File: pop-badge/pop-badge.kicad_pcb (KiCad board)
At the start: 2 copper layers, 129.5 x 101.3 mm, 164 parts, among them J1 Conn_01x05, Q1 S9013, Q2 AO3400A, U1 WS2812-2020, U10 WS2812-2020, U11 WS2812-2020, U12 WS2812-2020, U13 WS2812-2020, U14 WS2812-2020, U15 WS2812-2020, U16 WS2812-2020, U17 WS2812-2020, U18 WS2812-2020, U19 WS2812-2020, U2 WS2812-2020, U20 WS2812-2020, U21 WS2812-2020, U22 WS2812-2020, U23 WS2812-2020, U24 WS2812-2020, U25 WS2812-2020, U26 Pico, U3 WS2812-2020, U4 WS2812-2020, U5 WS2812-2020, U6 WS2812-2020, U7 WS2812-2020, U8 WS2812-2020, U9 WS2812-2020

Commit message: remove button label
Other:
- board text removed: "Button"
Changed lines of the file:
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@@
   (general
     (thickness 1.6)
-    (drawings 27)
+    (drawings 26)
     (tracks 737)
     (zones 0)
@@
       (drillshape 0)
       (scaleselection 1)
-      (outputdirectory ""))
+      (outputdirectory "gerbers"))
   )
   (net 0 "")
@@
     (effects (font (size 1 1) (thickness 0.15)) (justify mirror))
   )
-  (gr_text Button (at 56.134 120.018811 45) (layer B.SilkS)
-    (effects (font (size 0.8 0.8) (thickness 0.16)) (justify mirror))
-  )
   (gr_text LED- (at 53.848 119.762906 45) (layer B.SilkS)

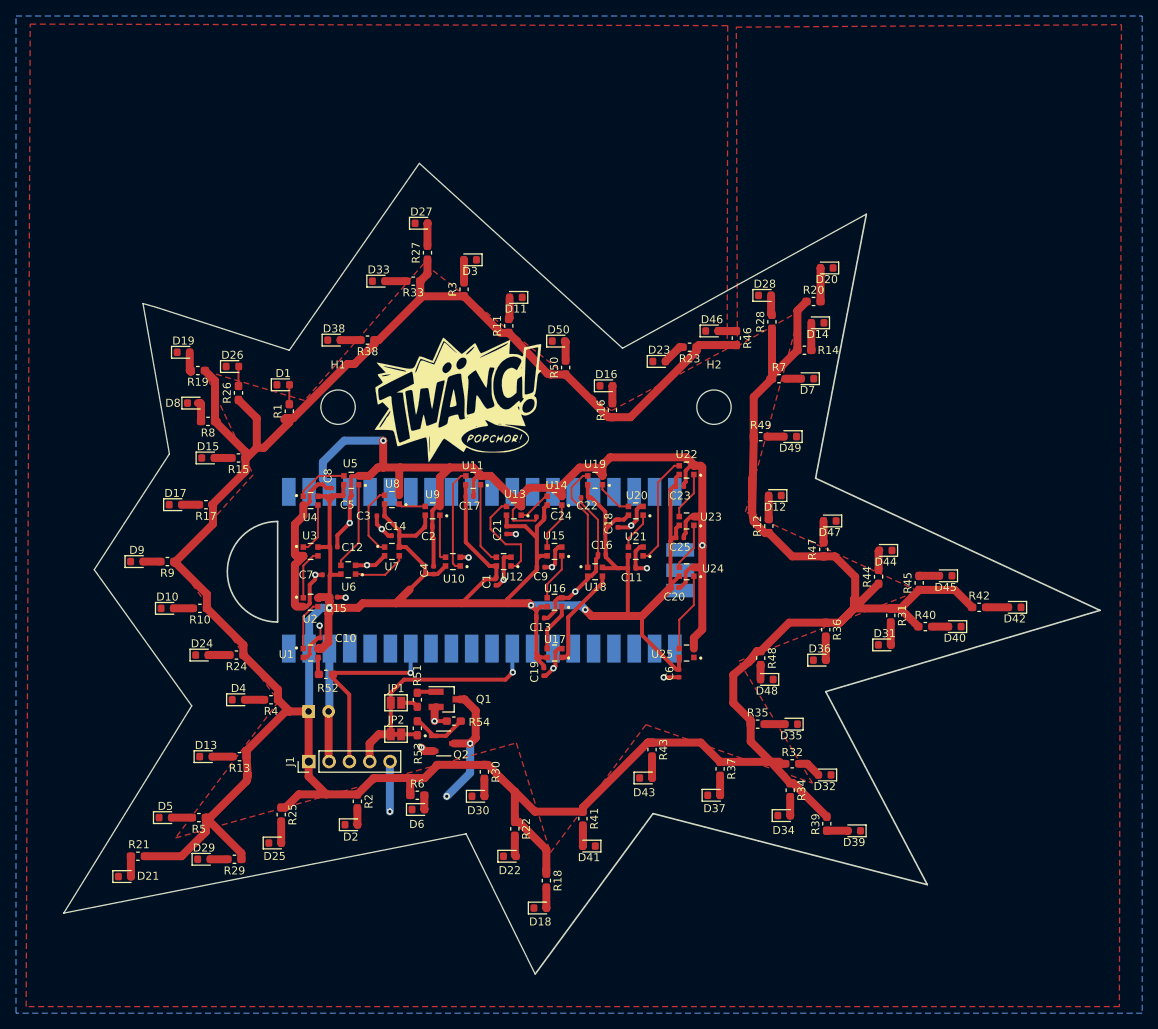
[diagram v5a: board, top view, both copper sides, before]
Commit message: renumber white leds
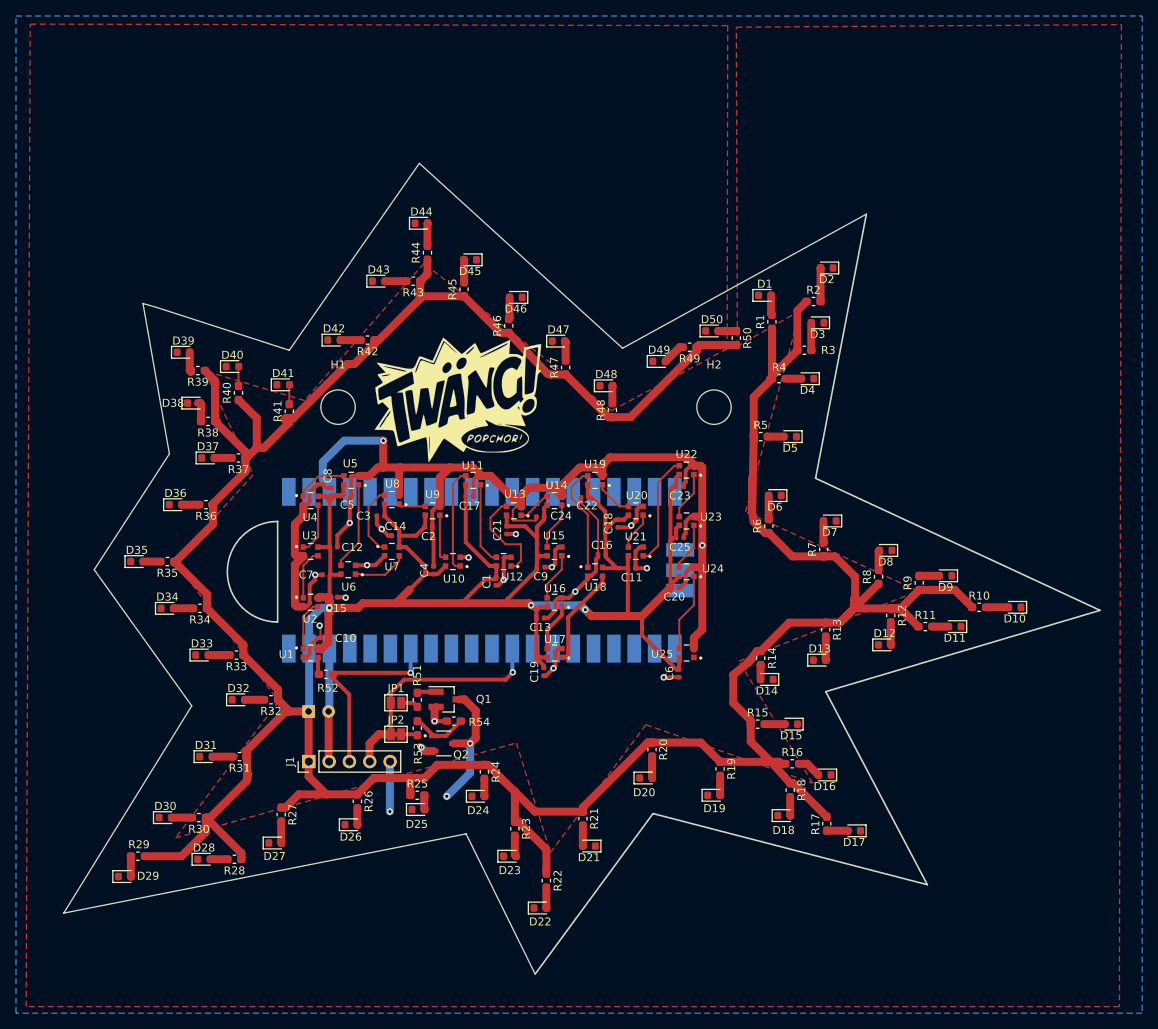
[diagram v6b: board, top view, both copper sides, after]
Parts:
- renumbered D28 to D1, D42 to D10, D40 to D11, D31 to D12, D36 to D13, D48 to D14, D35 to D15, D32 to D16, D39 to D17, D34 to D18, D37 to D19, D20 to D2, D43 to D20, D41 to D21, D18 to D22, D22 to D23, D30 to D24, D6 to D25, D2 to D26, D25 to D27, D29 to D28, D21 to D29, D14 to D3, D5 to D30, D13 to D31, D4 to D32, D24 to D33, D10 to D34, D9 to D35, D17 to D36, D15 to D37, D8 to D38, D19 to D39, D7 to D4, D26 to D40, D1 to D41, D38 to D42, D33 to D43, D27 to D44, D3 to D45, D11 to D46, D50 to D47, D16 to D48, D23 to D49, D49 to D5, D46 to D50, D12 to D6, D47 to D7, D44 to D8, D45 to D9, R28 to R1, R42 to R10, R40 to R11, R31 to R12, R36 to R13, R48 to R14, R35 to R15, R32 to R16, R39 to R17, R34 to R18, R37 to R19, R20 to R2, R43 to R20, R41 to R21, R18 to R22, R22 to R23, R30 to R24, R6 to R25, R2 to R26, R25 to R27, R29 to R28, R21 to R29, R14 to R3, R5 to R30, R13 to R31, R4 to R32, R24 to R33, R10 to R34, R9 to R35, R17 to R36, R15 to R37, R8 to R38, R19 to R39, R7 to R4, R26 to R40, R1 to R41, R38 to R42, R33 to R43, R27 to R44, R3 to R45, R11 to R46, R50 to R47, R16 to R48, R23 to R49, R49 to R5, R46 to R50, R12 to R6, R47 to R7, R44 to R8, R45 to R9
